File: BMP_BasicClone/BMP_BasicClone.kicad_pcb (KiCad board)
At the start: 2 copper layers, 42.1 x 116 mm, 57 parts, among them J1 BARREL_JACK, Q1 MMBT3904, Q2 MMBT3904, Q3 MMBT3904, Q4 MMBT3904

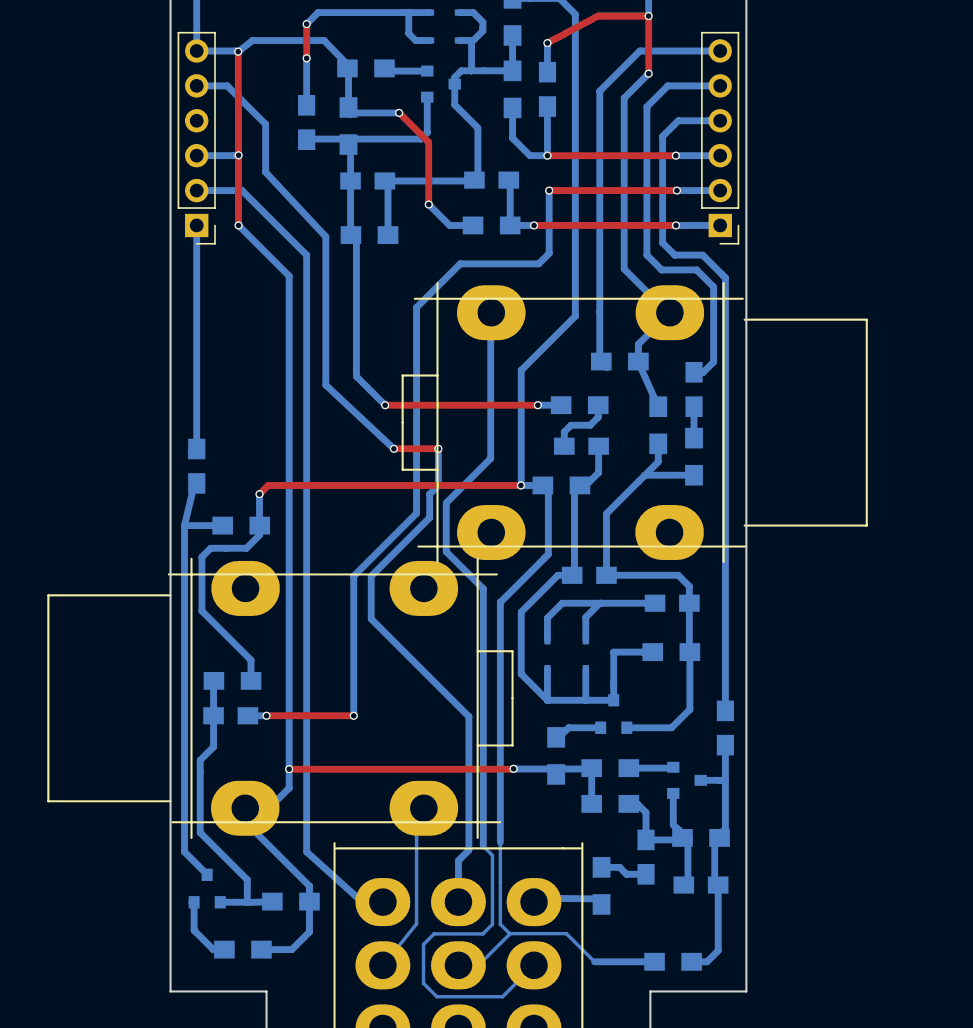
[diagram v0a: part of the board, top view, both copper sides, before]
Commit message: Moved sockets closer to  vertical edges
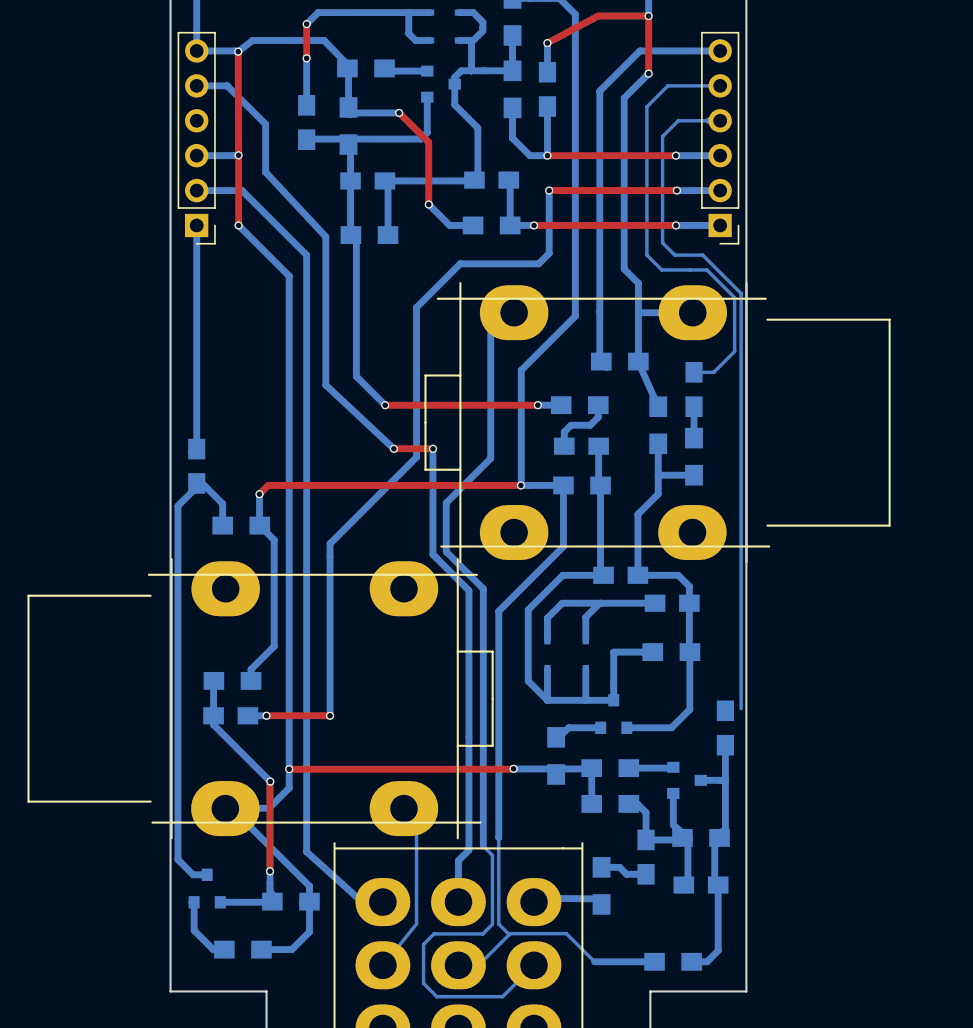
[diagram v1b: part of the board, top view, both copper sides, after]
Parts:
- moved C6 2.29 mm to (86.9, 158.6)
- moved J_IN1 1.66 mm to (85.6, 147.4)
- moved R10 1.50 mm to (84.0, 152.0)
- moved J_OUT1 1.45 mm to (64.6, 167.5)
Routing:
- net /LED_AN: track 75.2 -> 70.9 mm
- net Net-(C5-Pad2): track 36.5 -> 32.5 mm
- net /SUS_P2: track 30.1 -> 32.3 mm
- net Net-(C13-Pad1): track 32.5 -> 34.6 mm
- net Net-(C6-Pad1): track 39.2 -> 40.7 mm
- net /+9V: track 137.7 -> 136.2 mm
- net /TONE_P2: track 67.9 -> 66.9 mm
- net /GND: track 245.8 -> 245.2 mm
- net Net-(C12-Pad1): track 22.9 -> 22.7 mm, vias 0 -> 2
